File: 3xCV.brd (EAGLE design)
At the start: 98.1 x 50.2 mm, 84 parts, among them IC1 TL074, IC2 TL074, IC3 TL074, SW1 TL2285

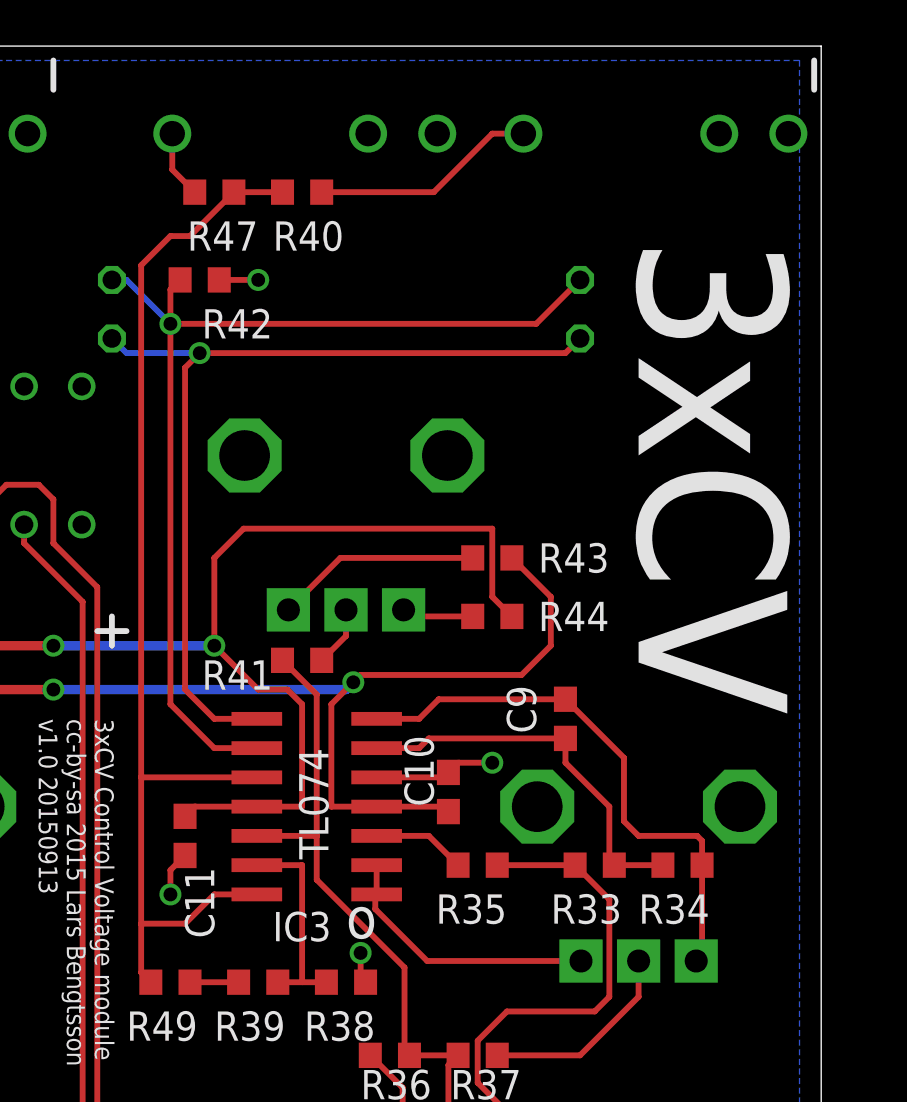
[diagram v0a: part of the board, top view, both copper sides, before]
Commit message: Added thru switch in unit 1, can switch output 1 to provide buffered output of unchanged input signal.
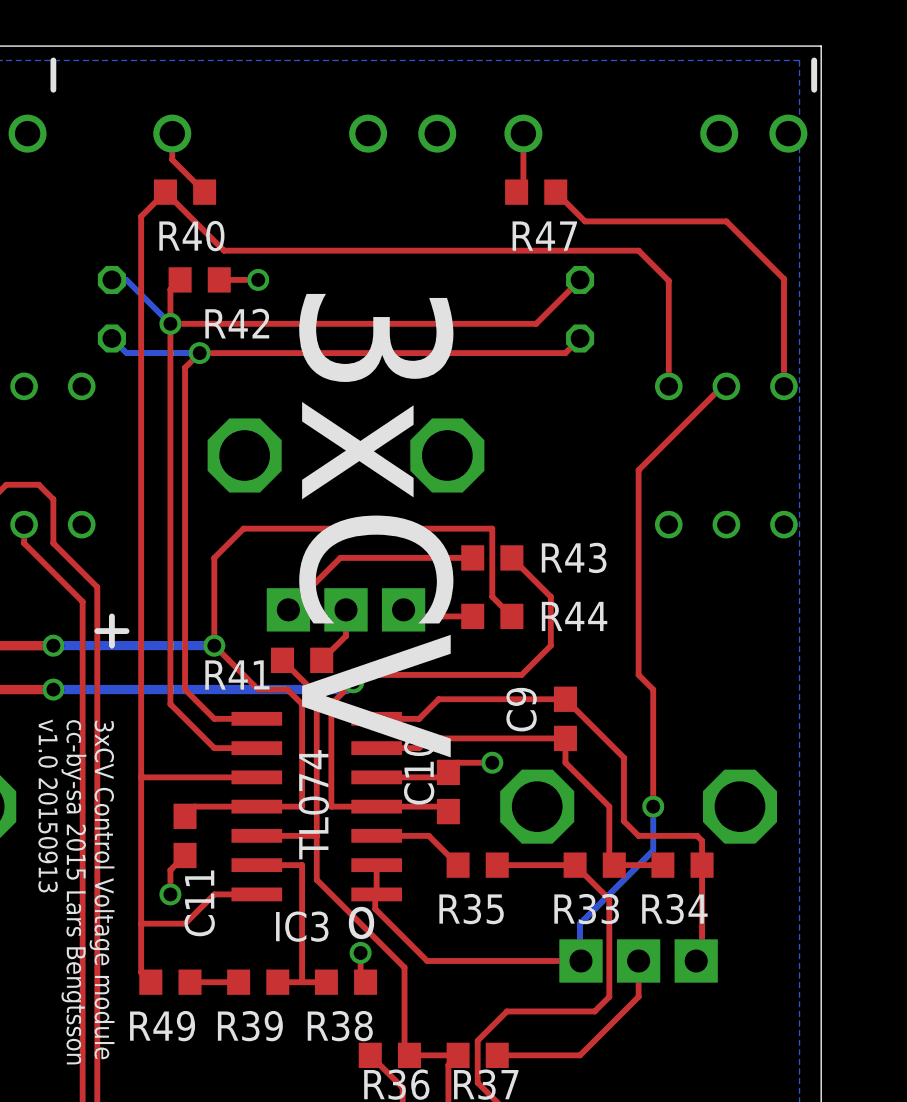
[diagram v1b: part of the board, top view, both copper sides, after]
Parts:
- added SW2: TL2285, lb_devs:TL2285_PCB
- moved OUT2 15.2 mm to (76.2, 52.1)
- moved OUT4 15.2 mm to (91.4, 52.1)
- moved R47 14.0 mm to (87.0, 49.5)
- moved R40 5.08 mm to (71.8, 49.5)
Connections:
- new net N$18: R47.1, SW2.4
- net N$42: now also SW2.5
- net N$47: now also SW2.6; no longer R47.1
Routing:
- net N$42: track 11.8 -> 40.0 mm, vias 0 -> 1
- net N$47: track 49.3 -> 73.5 mm
- net N$18: track 0.00 -> 16.1 mm
- net N$49: track 9.81 -> 3.12 mm
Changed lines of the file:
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@@
 <wire x1="1.905" y1="40.64" x2="2.54" y2="40.64" width="0.254" layer="25"/>
 <wire x1="2.54" y1="10.16" x2="1.905" y2="10.16" width="0.254" layer="25"/>
-<text x="91.44" y="47.625" size="6.4516" layer="25" font="vector" rot="SR270">3xCV</text>
+<text x="76.835" y="45.72" size="6.4516" layer="25" font="vector" rot="SR270">3xCV</text>
 <wire x1="28.575" y1="26.67" x2="29.845" y2="26.67" width="0.254" layer="25"/>
 <wire x1="31.75" y1="33.655" x2="31.75" y2="33.02" width="0.254" layer="25"/>
@@
 <element name="OUT" library="thonkiconn" package="WQP-PJ301M-12_JACK" value="WQP-PJ301M-12_JACK" x="10.16" y="52.07" rot="MR270"/>
 <element name="OUT1" library="thonkiconn" package="WQP-PJ301M-12_JACK" value="WQP-PJ301M-12_JACK" x="43.18" y="52.07" rot="MR270"/>
-<element name="OUT2" library="thonkiconn" package="WQP-PJ301M-12_JACK" value="WQP-PJ301M-12_JACK" x="91.44" y="52.07" rot="MR270"/>
+<element name="OUT2" library="thonkiconn" package="WQP-PJ301M-12_JACK" value="WQP-PJ301M-12_JACK" x="76.2" y="52.07" rot="MR270"/>
 <element name="R1" library="pot-alps" package="ALPS_POT_VERTICAL" value="100k" x="25.4" y="22.86" rot="MR180"/>
 <element name="R10" library="rcl" package="R0603" value="100k" x="12.7" y="15.24" smashed="yes" rot="R180">
@@
 </element>
 <element name="R4" library="pot-alps" package="ALPS_POT_VERTICAL" value="100k" x="45.72" y="38.1" rot="MR180"/>
-<element name="R40" library="rcl" package="R0603" value="220" x="76.835" y="49.53" smashed="yes">
-<attribute name="NAME" x="75.565" y="46.99" size="1.27" layer="25"/>
-<attribute name="VALUE" x="76.2" y="47.625" size="1.27" layer="27"/>
+<element name="R40" library="rcl" package="R0603" value="220" x="71.755" y="49.53" smashed="yes">
+<attribute name="NAME" x="70.485" y="46.99" size="1.27" layer="25"/>
+<attribute name="VALUE" x="71.12" y="47.625" size="1.27" layer="27"/>
 </element>
 <element name="R41" library="rcl" package="R0603" value="100k" x="76.835" y="29.21" smashed="yes" rot="R180">
@@
 <attribute name="VALUE" x="49.53" y="47.625" size="1.27" layer="27"/>
 </element>
-<element name="OUT4" library="thonkiconn" package="WQP-PJ301M-12_JACK" value="WQP-PJ301M-12_JACK" x="76.2" y="52.07" rot="MR270"/>
-<element name="R47" library="rcl" package="R0603" value="220" x="73.025" y="49.53" smashed="yes" rot="R180">
-<attribute name="NAME" x="74.93" y="48.26" size="1.27" layer="25" rot="R180"/>
-<attribute name="VALUE" x="73.66" y="51.435" size="1.27" layer="27" rot="R180"/>
+<element name="OUT4" library="thonkiconn" package="WQP-PJ301M-12_JACK" value="WQP-PJ301M-12_JACK" x="91.44" y="52.07" rot="MR270"/>
+<element name="R47" library="rcl" package="R0603" value="220" x="86.995" y="49.53" smashed="yes" rot="R180">
+<attribute name="NAME" x="88.9" y="48.26" size="1.27" layer="25" rot="R180"/>
+<attribute name="VALUE" x="87.63" y="51.435" size="1.27" layer="27" rot="R180"/>
 </element>
 <element name="OUT5" library="thonkiconn" package="WQP-PJ301M-12_JACK" value="WQP-PJ301M-12_JACK" x="25.4" y="52.07" rot="MR270"/>
@@
 </element>
 <element name="SW1" library="lb_devs" package="TL2285_PCB" value="TL2285" x="64.77" y="38.1" rot="MR0"/>
+<element name="SW2" library="lb_devs" package="TL2285_PCB" value="TL2285" x="95.25" y="38.1" rot="MR0"/>
 </elements>
 <signals>
@@
 <wire x1="80.01" y1="18.415" x2="80.01" y2="18.99" width="0.254" layer="1"/>
 <wire x1="80.01" y1="18.99" x2="80.07" y2="19.05" width="0.254" layer="1"/>
+<contactref element="SW2" pad="5"/>
+<wire x1="95.25" y1="41.1" x2="95.075" y2="41.1" width="0.254" layer="1"/>
+<wire x1="95.075" y1="41.1" x2="91.44" y2="37.465" width="0.254" layer="1"/>
+<wire x1="91.44" y1="37.465" x2="91.44" y2="28.575" width="0.254" layer="1"/>
+<wire x1="91.44" y1="28.575" x2="92.075" y2="27.94" width="0.254" layer="1"/>
+<wire x1="92.075" y1="27.94" x2="92.075" y2="22.86" width="0.254" layer="1"/>
+<via x="92.075" y="22.86" extent="1-16" drill="0.6" shape="octagon"/>
+<wire x1="92.075" y1="22.86" x2="92.075" y2="20.955" width="0.254" layer="16"/>
+<wire x1="92.075" y1="20.955" x2="88.9" y2="17.78" width="0.254" layer="16"/>
+<wire x1="88.9" y1="17.78" x2="88.9" y2="16.2" width="0.254" layer="16"/>
+<wire x1="88.9" y1="16.2" x2="88.94" y2="16.16" width="0.254" layer="16"/>
 </signal>
 <signal name="N$43">
@@
 <wire x1="69.85" y1="24.13" x2="69.85" y2="17.78" width="0.254" layer="1"/>
 <wire x1="69.85" y1="17.78" x2="69.85" y2="15.66" width="0.254" layer="1"/>
-<contactref element="R47" pad="1"/>
 <contactref element="R49" pad="1"/>
 <wire x1="69.85" y1="15.66" x2="70.27" y2="15.24" width="0.254" layer="1"/>
 <wire x1="73.025" y1="19.05" x2="71.755" y2="17.78" width="0.254" layer="1"/>
 <wire x1="71.755" y1="17.78" x2="69.85" y2="17.78" width="0.254" layer="1"/>
-<wire x1="69.85" y1="24.13" x2="69.85" y2="46.355" width="0.254" layer="1"/>
-<wire x1="75.985" y1="49.53" x2="73.875" y2="49.53" width="0.254" layer="1"/>
-<wire x1="69.85" y1="46.355" x2="71.12" y2="47.625" width="0.254" layer="1"/>
-<wire x1="71.12" y1="47.625" x2="71.97" y2="47.625" width="0.254" layer="1"/>
-<wire x1="71.97" y1="47.625" x2="73.875" y2="49.53" width="0.254" layer="1"/>
+<wire x1="69.85" y1="24.13" x2="69.85" y2="48.475" width="0.254" layer="1"/>
+<contactref element="SW2" pad="6"/>
+<wire x1="69.85" y1="48.475" x2="70.905" y2="49.53" width="0.254" layer="1"/>
+<wire x1="92.75" y1="41.1" x2="92.75" y2="45.68" width="0.254" layer="1"/>
+<wire x1="92.75" y1="45.68" x2="91.44" y2="46.99" width="0.254" layer="1"/>
+<wire x1="91.44" y1="46.99" x2="73.445" y2="46.99" width="0.254" layer="1"/>
+<wire x1="73.445" y1="46.99" x2="70.905" y2="49.53" width="0.254" layer="1"/>
 </signal>
 <signal name="N$48">
@@
 <contactref element="OUT2" pad="P$1"/>
 <contactref element="R40" pad="2"/>
-<wire x1="86.44" y1="52.07" x2="85.09" y2="52.07" width="0.254" layer="1"/>
-<wire x1="85.09" y1="52.07" x2="82.55" y2="49.53" width="0.254" layer="1"/>
-<wire x1="82.55" y1="49.53" x2="77.685" y2="49.53" width="0.254" layer="1"/>
+<wire x1="71.2" y1="52.07" x2="71.2" y2="50.935" width="0.254" layer="1"/>
+<wire x1="71.2" y1="50.935" x2="72.605" y2="49.53" width="0.254" layer="1"/>
 </signal>
 <signal name="N$50">
@@
 <contactref element="R47" pad="2"/>
 <contactref element="OUT4" pad="P$1"/>
-<wire x1="71.2" y1="52.07" x2="71.2" y2="50.505" width="0.254" layer="1"/>
-<wire x1="71.2" y1="50.505" x2="72.175" y2="49.53" width="0.254" layer="1"/>
+<wire x1="86.44" y1="52.07" x2="86.44" y2="49.825" width="0.254" layer="1"/>
+<wire x1="86.44" y1="49.825" x2="86.145" y2="49.53" width="0.254" layer="1"/>
 </signal>
 <signal name="N$56">
@@
 <wire x1="74.08" y1="15.24" x2="71.97" y2="15.24" width="0.254" layer="1"/>
 </signal>
+<signal name="N$18">
+<contactref element="SW2" pad="4"/>
+<contactref element="R47" pad="1"/>
+<wire x1="97.75" y1="41.1" x2="97.75" y2="45.76" width="0.254" layer="1"/>
+<wire x1="97.75" y1="45.76" x2="95.25" y2="48.26" width="0.254" layer="1"/>
+<wire x1="95.25" y1="48.26" x2="89.115" y2="48.26" width="0.254" layer="1"/>
+<wire x1="89.115" y1="48.26" x2="87.845" y2="49.53" width="0.254" layer="1"/>
+</signal>
 </signals>
